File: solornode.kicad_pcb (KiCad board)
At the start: 2 copper layers, 77 parts, among them J1 Conn_01x06, Q1 Q_NMOS_GDS, Q4 Q_PNP_BCE, Q5 Q_NPN_BCE, SW1 SW_Push, U1 LM358, U2 OC5864, U3 PY32F003F1xUx, U4 MAX485E, U5 SGM2033-5.0

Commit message: PCB布局，划定边框
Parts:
- C6, C7, D2, D3, NT1, NT2, Q4, Q5, R1, R13, R14, R15, R16, R2: moved to B.Cu
- moved GD3 46.5 mm to (145.8, 60.1)
- moved GD2 45.3 mm to (145.8, 64.8)
- moved GD1 43.1 mm to (145.8, 69.3)
- moved R10 41.0 mm to (133.9, 67.5), turned to 90 degrees
- moved R9 40.9 mm to (133.6, 65.7), turned to 180 degrees
- moved R12 38.4 mm to (132.9, 67.5), turned to -90 degrees
- moved R11 37.4 mm to (130.7, 64.3), turned to 180 degrees
- moved C5 31.8 mm to (130.7, 70.8), turned to 180 degrees
- moved U1 30.6 mm to (128.8, 67.5), turned to 0 degrees
- moved R8 25.4 mm to (124.5, 66.1), turned to 90 degrees
- moved C16 22.7 mm to (132.0, 84.5)
- moved C17 22.7 mm to (125.8, 84.5)
- moved U5 22.7 mm to (128.9, 84.5)
- moved R7 22.5 mm to (122.9, 66.6), turned to 0 degrees
- moved R6 21.9 mm to (124.4, 68.8), turned to -90 degrees
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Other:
- board outline added: 35.9 x 42.4 mm

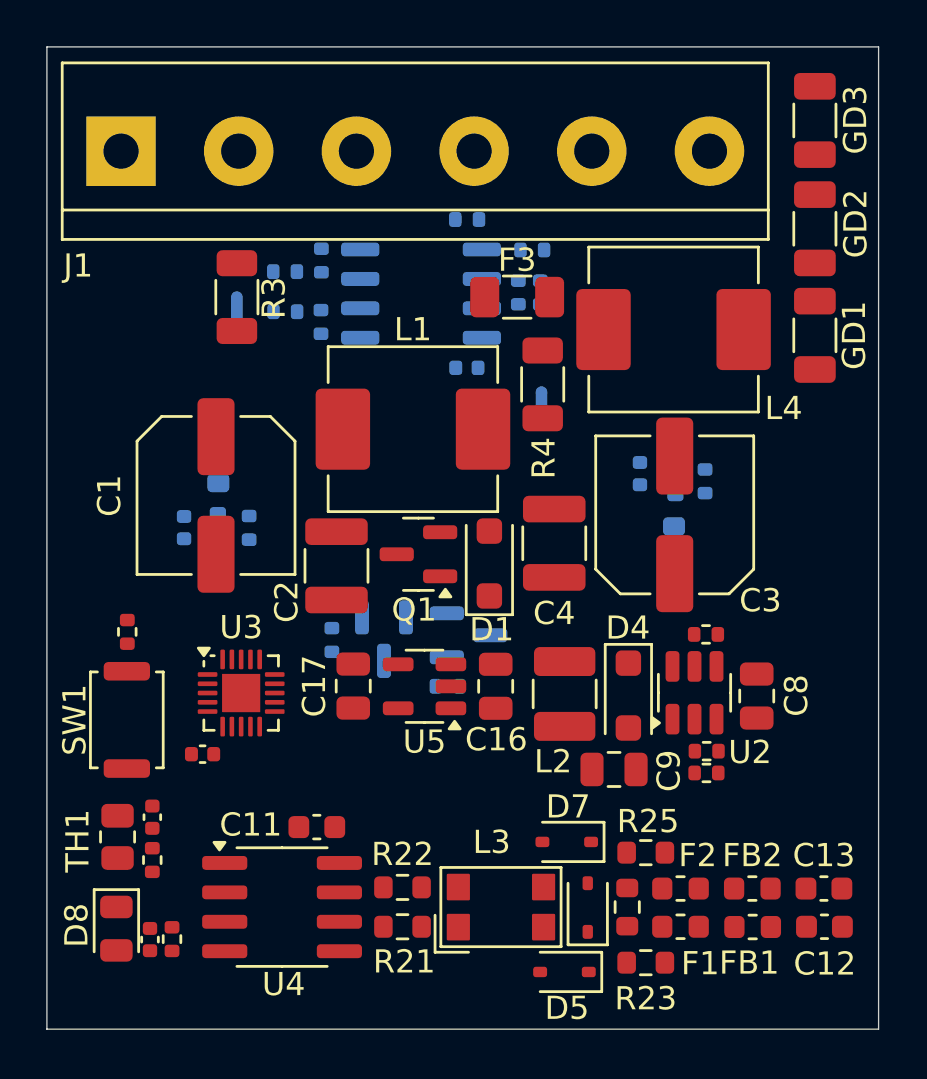
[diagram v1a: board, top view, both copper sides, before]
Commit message: 初步布线，添加覆铜
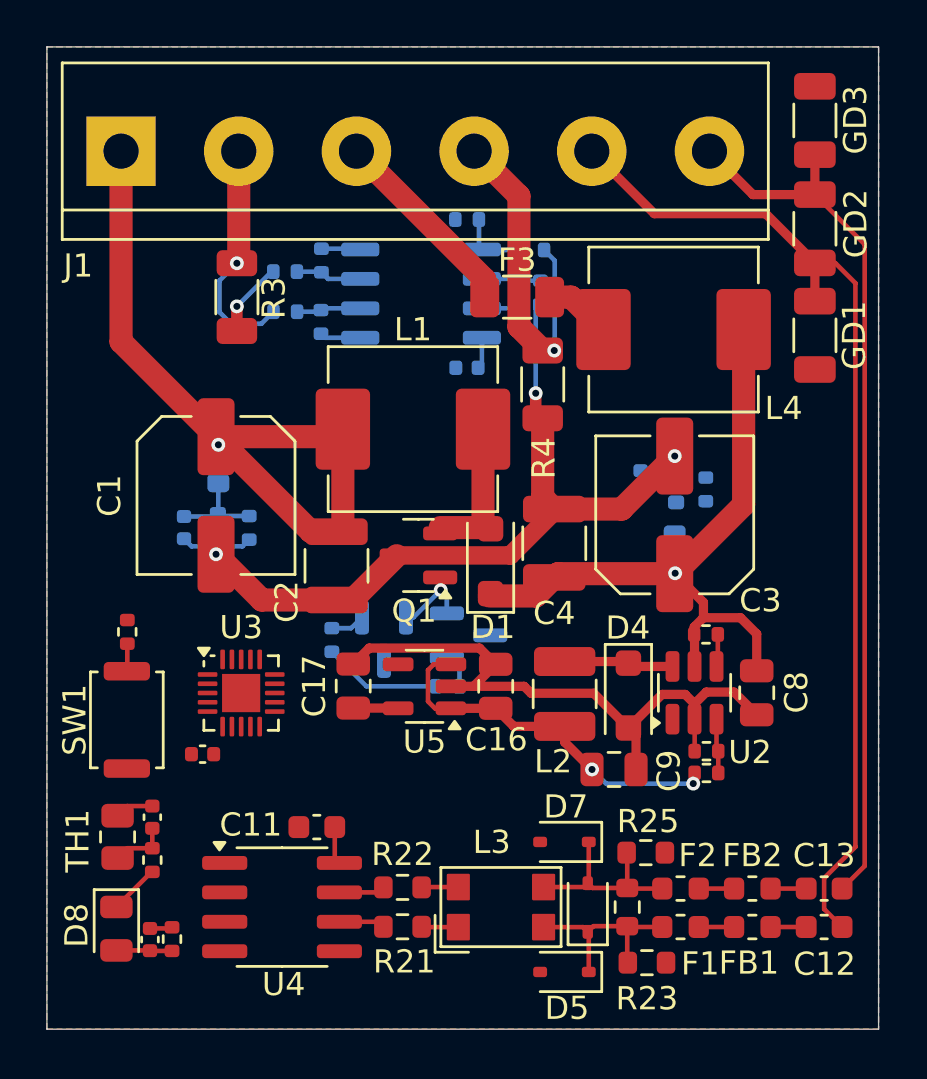
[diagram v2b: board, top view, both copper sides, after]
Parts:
- NT1, NT2: moved to F.Cu
- moved NT2 0.40 mm to (120.8, 68.6)
- moved C7 0.35 mm to (138.2, 75.7)
- moved R15 0.35 mm to (139.7, 78.8)
- moved D3 0.35 mm to (139.8, 75.9)
- moved R16 0.35 mm to (141.0, 76.0)
- moved NT1 0.25 mm to (133.7, 72.3)
- moved C8 0.14 mm to (143.2, 84.8)
- moved D1 0.11 mm to (131.8, 79.1)
- moved D7 0.10 mm to (134.9, 91.2)
- moved R23 0.05 mm to (138.5, 96.4)
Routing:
- net GND: track 0.00 -> 62.2 mm, vias 0 -> 2
- net /485+: track 0.00 -> 44.1 mm
- net /485-: track 0.00 -> 38.3 mm
- net /SLR+: track 0.00 -> 30.9 mm, vias 0 -> 1
- net VINP: track 0.00 -> 29.0 mm, vias 0 -> 1
- net /Vdco: track 0.00 -> 16.2 mm, vias 0 -> 2
- net /BUS-: track 0.00 -> 14.4 mm, vias 0 -> 1
- net /SLR-: track 0.00 -> 10.0 mm, vias 0 -> 1
- net Net-(D5-K): track 0.00 -> 8.66 mm
- net Net-(D6-A): track 0.00 -> 8.62 mm
- net Net-(J1-Pin_3): track 0.00 -> 8.59 mm
- net Net-(D1-A): track 0.00 -> 6.20 mm
- net /MOS_DrvIn: track 0.00 -> 5.11 mm
- net Net-(D4-K): track 0.00 -> 4.74 mm
- net /ADC_Vslr: track 0.00 -> 4.24 mm
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- added copper zone on B.Cu, net GND
- added copper zone on F.Cu, net GND

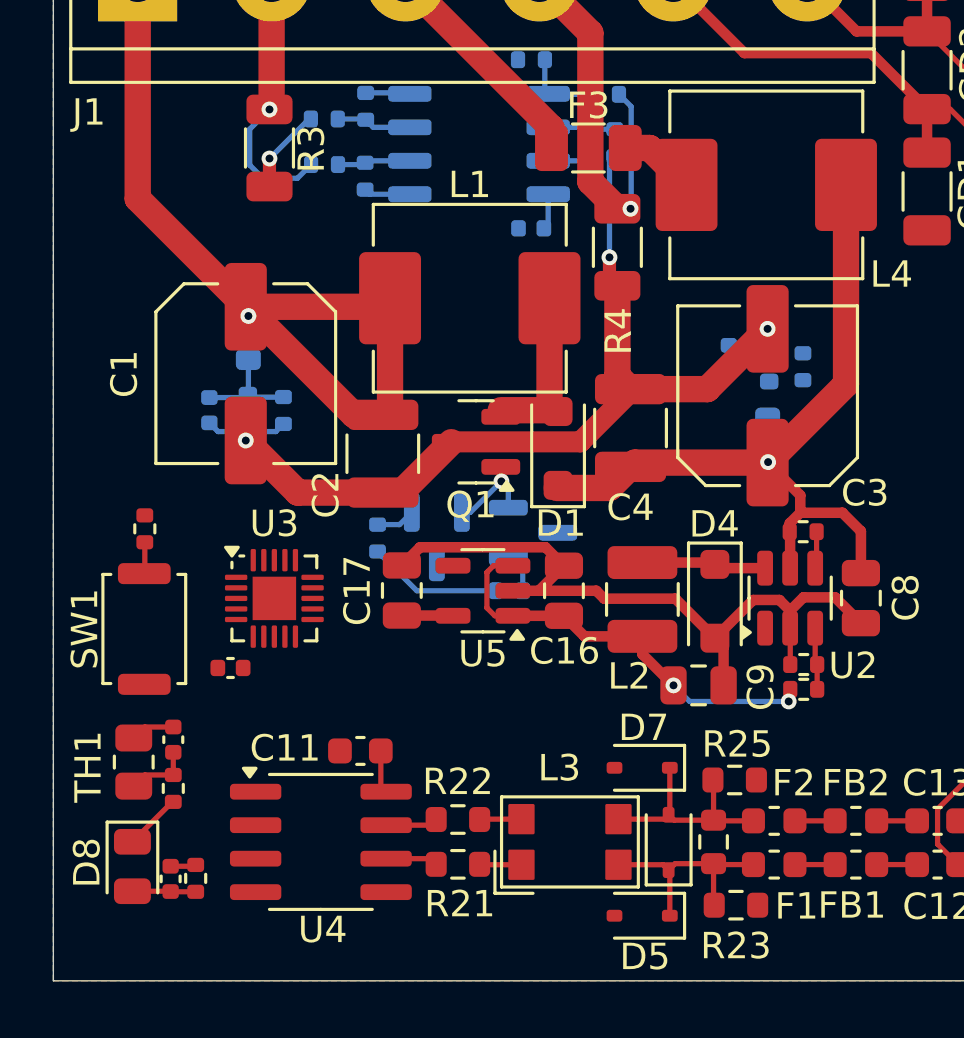
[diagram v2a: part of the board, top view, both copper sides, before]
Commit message: 配置MCU引脚并连接
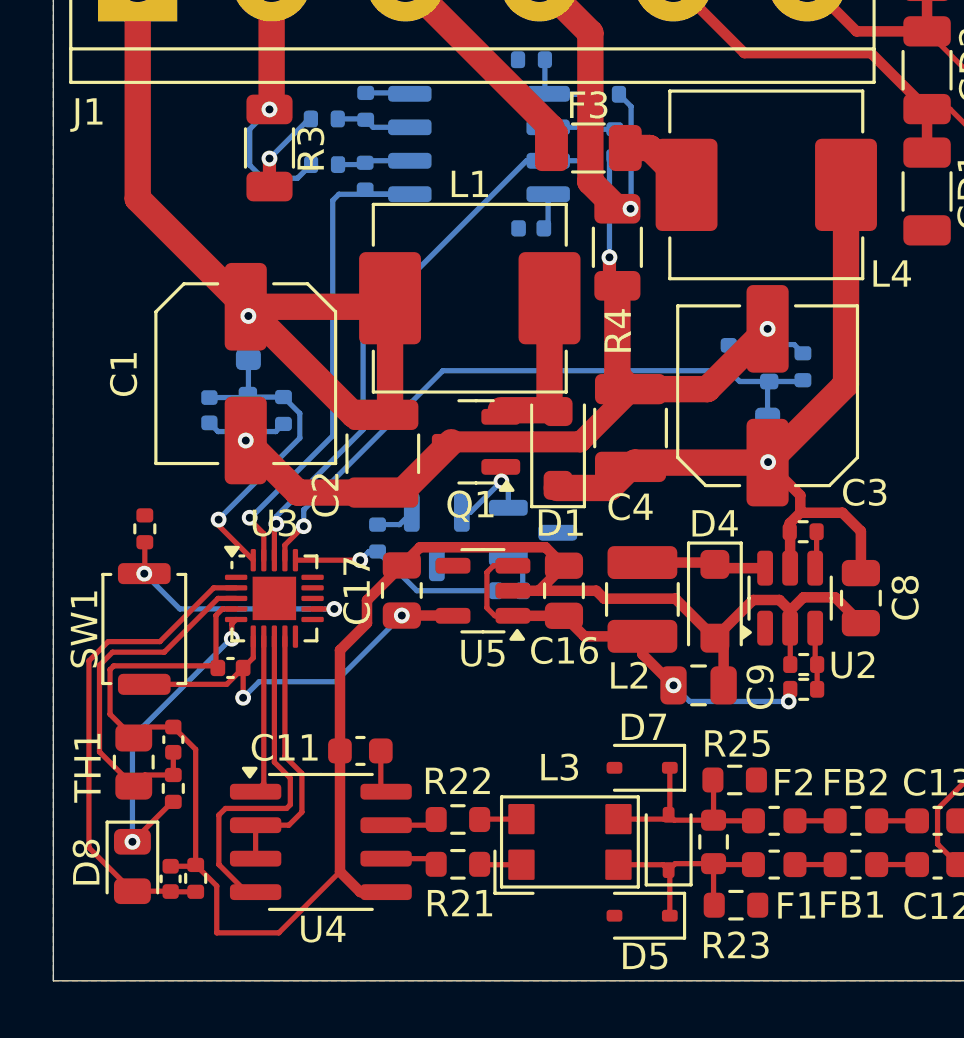
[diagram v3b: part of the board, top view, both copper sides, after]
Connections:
- U3 pad 11: /MAX485_RO -> /I2C_SDA
- U3 pad 16: unconnected-(U3-PA0-Pad16) -> /MOS_DrvIn
- U3 pad 17: unconnected-(U3-PA1-Pad17) -> /ADC_Vbus
- U3 pad 18: unconnected-(U3-PA2-Pad18) -> /ADC_Ibus
- U3 pad 19: unconnected-(U3-PA3-Pad19) -> /ADC_Islr
- U3 pad 2: unconnected-(U3-PA6-Pad2) -> /ADC_PD
- U3 pad 20: unconnected-(U3-PA4-Pad20) -> /ADC_Vslr
- U3 pad 3: unconnected-(U3-PA7-Pad3) -> /ADC_T
- U3 pad 5: unconnected-(U3-PA12-Pad5) -> /SampEn
- U3 pad 7: unconnected-(U3-PA13_SWD-Pad7) -> /MAX485_RO
- U3 pad 8: unconnected-(U3-PA14_SWC-Pad8) -> /MAX485_DI
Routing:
- net GND: track 62.2 -> 104.6 mm
- net /ADC_Vbus: track 0.00 -> 24.9 mm, vias 0 -> 1
- net /ADC_Ibus: track 1.65 -> 21.6 mm, vias 0 -> 1
- net /ADC_Islr: track 1.77 -> 20.0 mm, vias 0 -> 1
- net /ADC_PD: track 2.41 -> 18.6 mm
- net +3.3V: track 1.94 -> 15.7 mm, vias 0 -> 2
- net /MAX485_DI: track 0.00 -> 13.2 mm
- net /ADC_T: track 2.54 -> 13.9 mm
- net /MAX485_TR: track 0.00 -> 10.2 mm
- net /SampEn: track 2.18 -> 12.3 mm, vias 0 -> 2
- net /PUSH: track 1.20 -> 9.79 mm, vias 0 -> 2
- net /ADC_Vslr: track 4.24 -> 12.5 mm, vias 0 -> 1
- net /MAX485_RO: track 0.00 -> 6.01 mm
- net /MOS_DrvIn: track 5.11 -> 8.36 mm, vias 0 -> 1
